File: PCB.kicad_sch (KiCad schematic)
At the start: 21 parts, among them SW1 RotaryEncoder, SW2 RotaryEncoder_Switch, U2 MOUDLE-SEEEDUINO-XIAO

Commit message: New changes
alot and not much has happened
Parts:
- removed D5: D_Small, symbol Device:D_Small
- removed MX7: MX-NoLED, symbol MX_Alps_Hybrid:MX-NoLED
- removed SW1: RotaryEncoder, symbol Device:RotaryEncoder
- added SW1: RotaryEncoder_Switch, symbol Device:RotaryEncoder_Switch
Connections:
- net COL0: now also U2.4 (PA11_A3_D3)
- net COL1: now also U2.5 (PA8_A4_D4_SDA)
- net ROW0: now also U2.1 (PA02_A0_D0)
- net ROW1: now also U2.2 (PA4_A1_D1)
- net ROW2: now also U2.3 (PA10_A2_D2)
- net at MX3.2 (ROW): now also D3.2 (A)
- net COL2: now reaches U2.6 (PA9_A5_D5_SCL)
- net COL2: now also MX10.1 (COL), MX9.1 (COL)

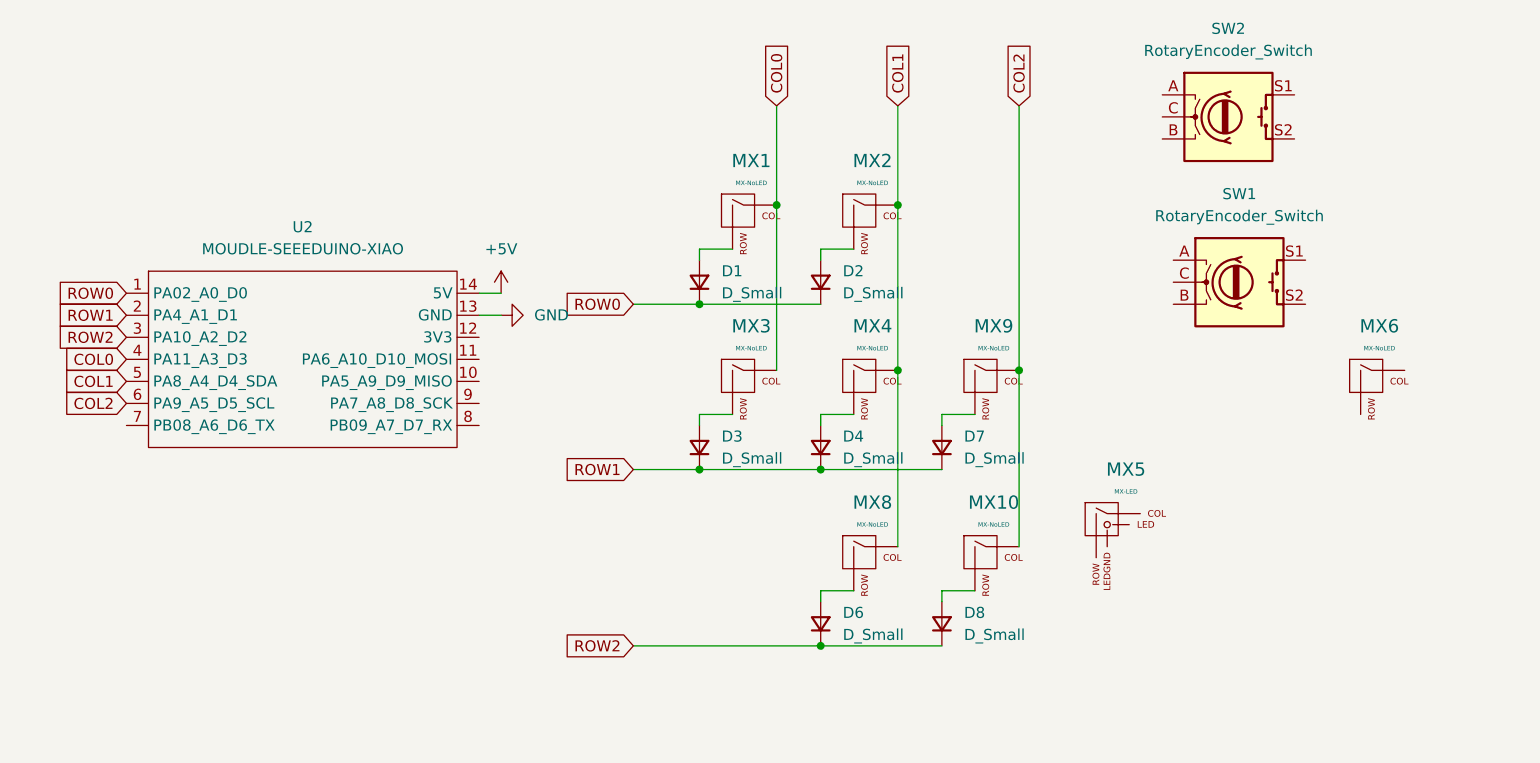
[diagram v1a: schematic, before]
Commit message: Assigning footprints
tried to finish this before the end but couldn't :(. I couldn't find the rp2040 with holes footprint.

I will still continue designing the other parts.
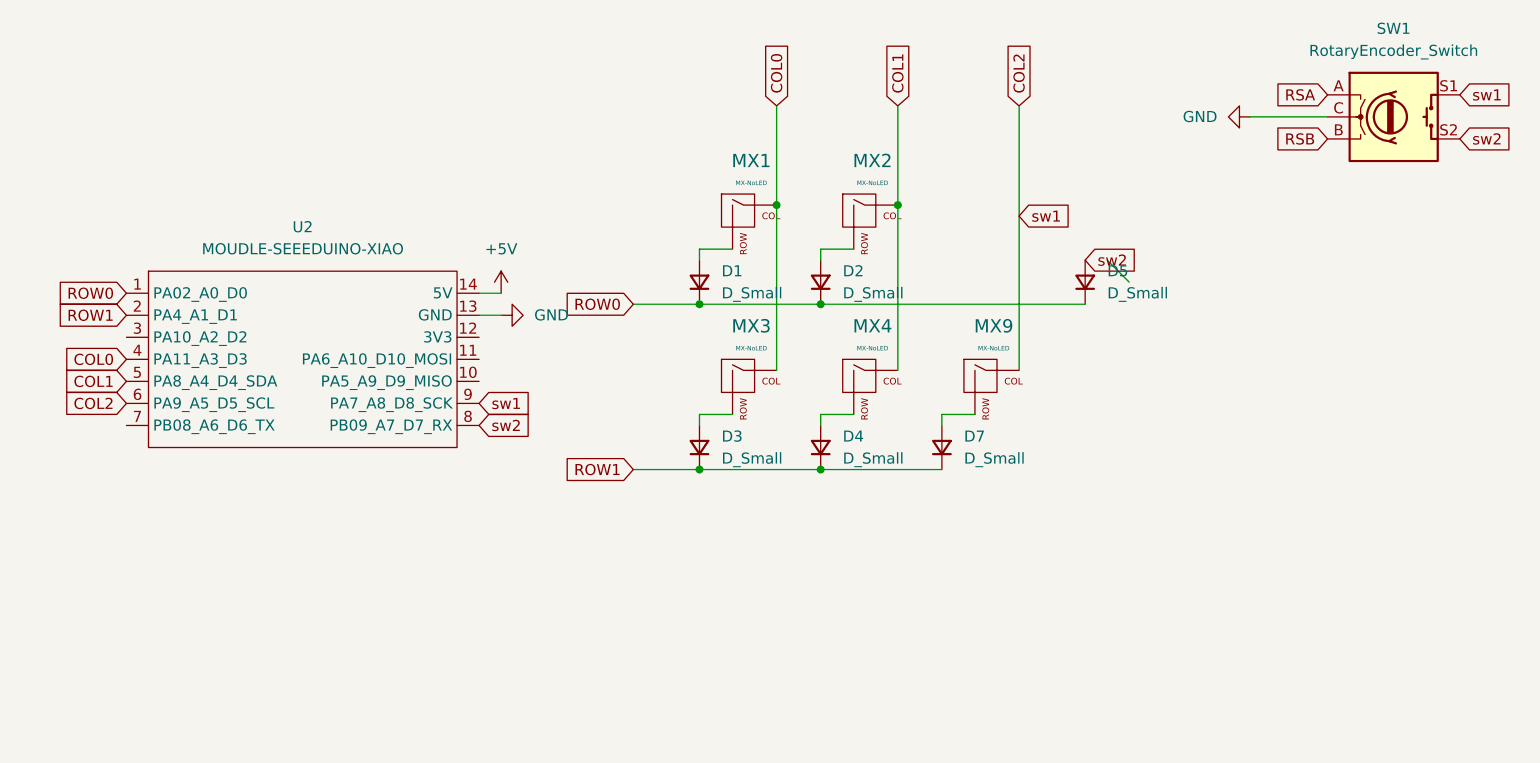
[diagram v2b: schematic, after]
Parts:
- removed D6, D8: D_Small, symbol Device:D_Small
- removed MX10, MX6, MX8: MX-NoLED, symbol MX_Alps_Hybrid:MX-NoLED
- removed MX5: MX-LED, symbol MX_Alps_Hybrid:MX-LED
- removed SW2: RotaryEncoder_Switch, symbol Device:RotaryEncoder_Switch
- added D5: D_Small, Diode_SMD:D_0201_0603Metric, symbol Device:D_Small
- D1, D2, D3, D4, D7: footprint (none) -> Diode_SMD:D_0201_0603Metric
- MX1, MX2, MX3, MX4, MX9: footprint (none) -> MX_Alps_Hybrid:MX-1.5U-NoLED
- SW1: footprint (none) -> Rotary_Encoder:RotaryEncoder_Alps_EC11E-Switch_Vertical_H20mm
- U2: footprint (none) -> Seeed Studio XIAO Series Library:XIAO-RP2040-SMD
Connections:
- net COL2: now also SW1.S1, U2.9 (PA7_A8_D8_SCK)
- net GND: now also SW1.C
- net ROW0: now also D5.1 (K)
- net sw2: now reaches U2.8 (PB09_A7_D7_RX)
- net sw2: now also SW1.S2, D5.2 (A)
- net RSA: now reaches SW1.A
- net RSB: now reaches SW1.B
- net ROW2: no longer names the net of U2.3 (PA10_A2_D2)
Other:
- moved on the sheet: SW1

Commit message: update to pcb and schematic
made with following the guide. will change to make my own
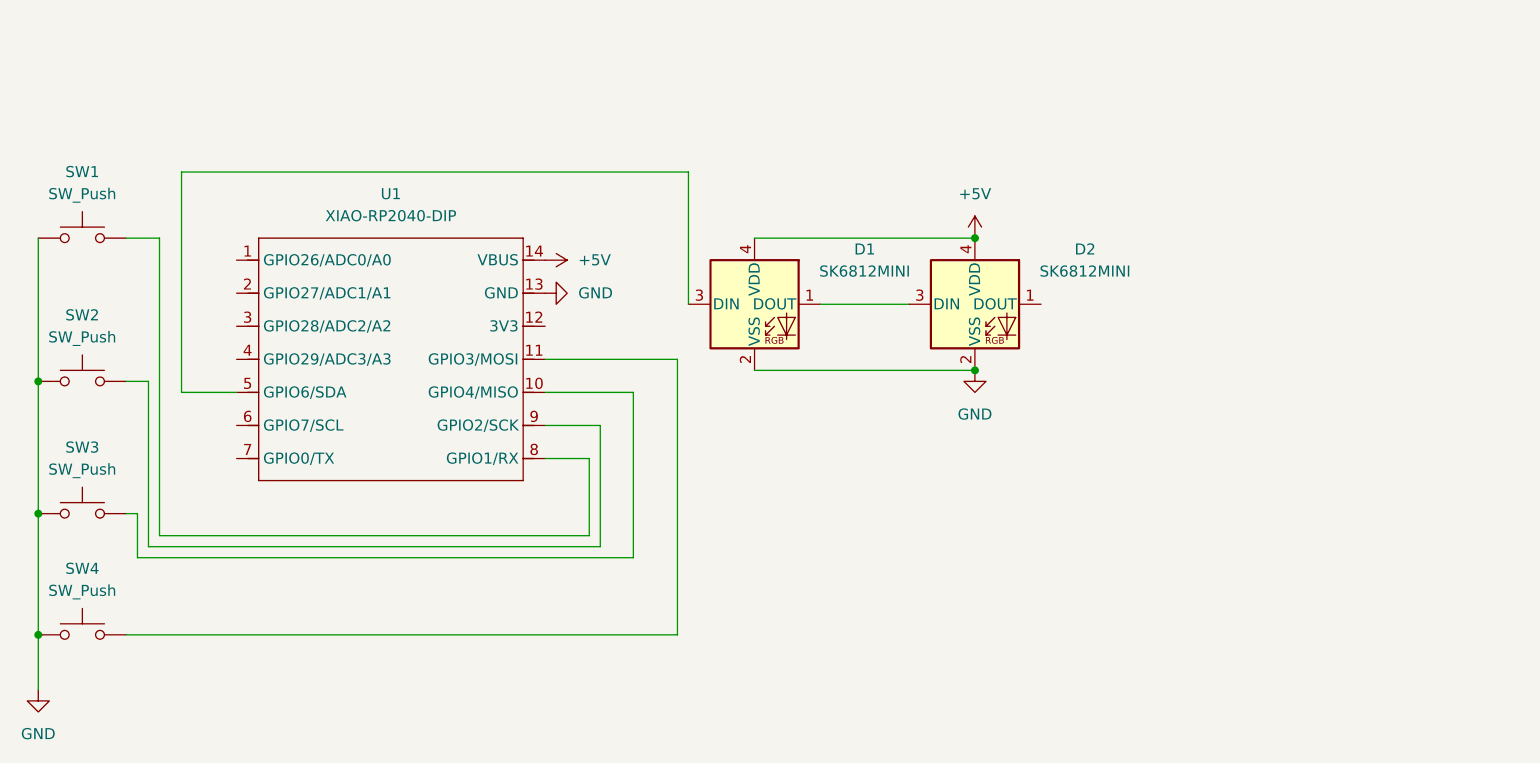
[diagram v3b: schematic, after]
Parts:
- removed D1, D2, D3, D4, D5, D7: D_Small, Diode_SMD:D_0201_0603Metric, symbol Device:D_Small
- removed MX1, MX2, MX3, MX4, MX9: MX-NoLED, MX_Alps_Hybrid:MX-1.5U-NoLED, symbol MX_Alps_Hybrid:MX-NoLED
- removed SW1: RotaryEncoder_Switch, Rotary_Encoder:RotaryEncoder_Alps_EC11E-Switch_Vertical_H20mm, symbol Device:RotaryEncoder_Switch
- removed U2: MOUDLE-SEEEDUINO-XIAO, Seeed Studio XIAO Series Library:XIAO-RP2040-SMD, symbol MOUDLE-SEEEDUINO-XIAO:MOUDLE-SEEEDUINO-XIAO
- added D1, D2: SK6812MINI, LED_SMD:LED_SK6812MINI_PLCC4_3.5x3.5mm_P1.75mm, symbol LED:SK6812MINI
- added SW1, SW2, SW3, SW4: SW_Push, Button_Switch_Keyboard:SW_Cherry_MX_1.00u_PCB, symbol Switch:SW_Push
- added U1: XIAO-RP2040-DIP, Seeed Studio XIAO Series Library:XIAO-RP2040-DIP, symbol Seeed_Studio_XIAO_Series:XIAO-RP2040-DIP
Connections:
- net +5V: now also D1.4 (VDD), D2.4 (VDD), U1.14 (VBUS)
- net GND: now also D1.2 (VSS), D2.2 (VSS), SW1.1, SW2.1, SW3.1, SW4.1, U1.13 (GND)
- new net: SW2.2, U1.9 (GPIO2/SCK)
- new net: D1.1 (DOUT), D2.3 (DIN)
- new net: SW1.2, U1.8 (GPIO1/RX)
- new net: SW3.2, U1.10 (GPIO4/MISO)
- new net: SW4.2, U1.11 (GPIO3/MOSI)
- new net: D1.3 (DIN), U1.5 (GPIO6/SDA)
